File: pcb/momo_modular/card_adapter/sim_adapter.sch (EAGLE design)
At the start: 6 parts, among them U1 ESDA6V1SC6

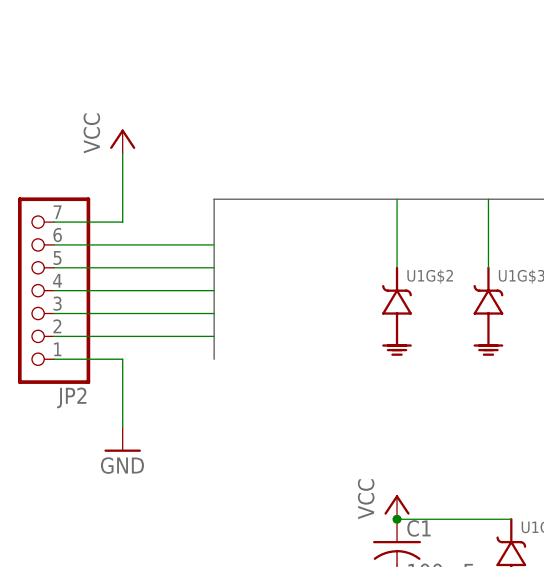
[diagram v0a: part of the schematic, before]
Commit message: Finalize sd/sim card adapter board
- make size a round number
- make pinout standard for minimal wiring
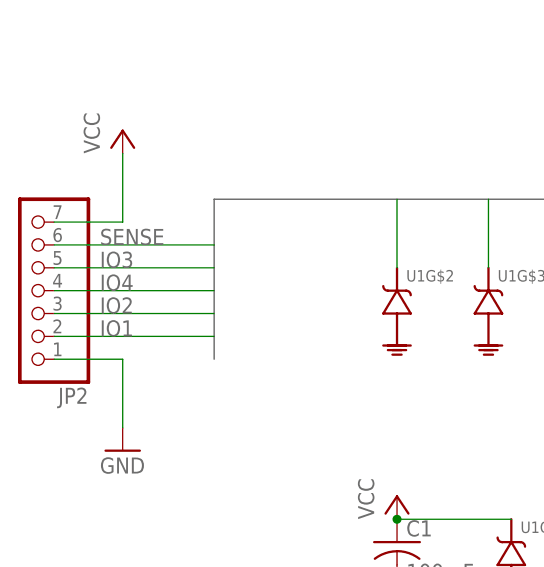
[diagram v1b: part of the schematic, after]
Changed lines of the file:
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@@
 <?xml version="1.0" encoding="utf-8"?>
 <!DOCTYPE eagle SYSTEM "eagle.dtd">
-<eagle version="6.5.0">
+<eagle version="6.4">
 <drawing>
 <settings>
@@
 <pinref part="JP2" gate="A" pin="2"/>
 <wire x1="33.02" y1="106.68" x2="15.24" y2="106.68" width="0.1524" layer="91"/>
+<label x="20.32" y="106.68" size="1.778" layer="95"/>
 </segment>
 </net>
@@
 <pinref part="JP2" gate="A" pin="3"/>
 <wire x1="33.02" y1="109.22" x2="15.24" y2="109.22" width="0.1524" layer="91"/>
+<label x="20.32" y="109.22" size="1.778" layer="95"/>
 </segment>
 </net>
@@
 <pinref part="JP2" gate="A" pin="5"/>
 <wire x1="33.02" y1="114.3" x2="15.24" y2="114.3" width="0.1524" layer="91"/>
+<label x="20.32" y="114.3" size="1.778" layer="95"/>
 </segment>
 </net>
@@
 <pinref part="JP2" gate="A" pin="4"/>
 <wire x1="33.02" y1="111.76" x2="15.24" y2="111.76" width="0.1524" layer="91"/>
+<label x="20.32" y="111.76" size="1.778" layer="95"/>
 </segment>
 </net>
@@
 <pinref part="JP2" gate="A" pin="6"/>
 <wire x1="33.02" y1="116.84" x2="15.24" y2="116.84" width="0.1524" layer="91"/>
-</segment>
-</net>
+<label x="20.32" y="116.84" size="1.778" layer="95"/>
+</segment>
+</net>

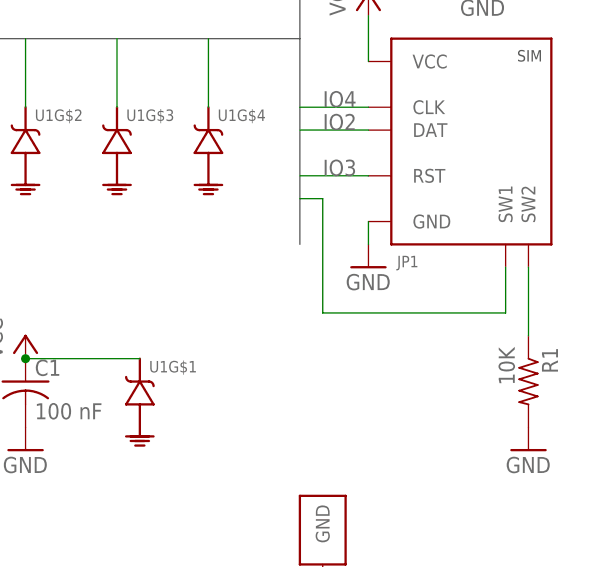
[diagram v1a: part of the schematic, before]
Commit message: Add final wire for sensing sim insertion
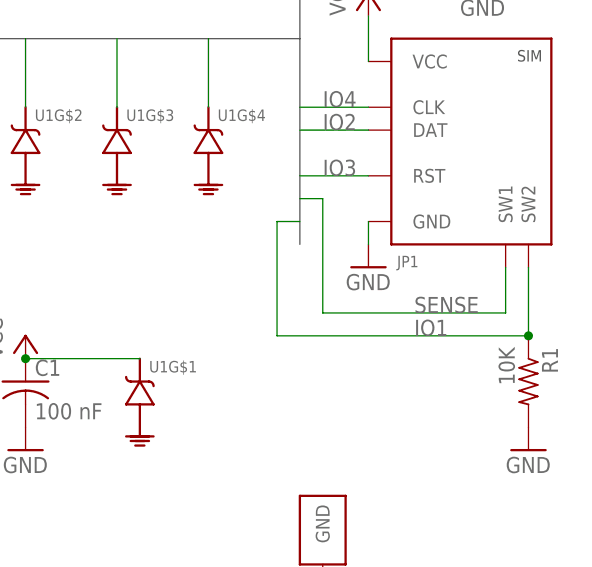
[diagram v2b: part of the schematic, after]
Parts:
- C1: DIGIKEY-PN (none) -> 445-1265-1-ND
- JP3: POPULATE-SIM (none) -> no
- R1: DIGIKEY-PN (none) -> P10.0KHCT-ND
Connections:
- removed net N$1: JP1.SW2, R1.1
- net IO1: now also JP1.SW2, R1.1
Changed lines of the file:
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@@
 <?xml version="1.0" encoding="utf-8"?>
 <!DOCTYPE eagle SYSTEM "eagle.dtd">
-<eagle version="6.4">
+<eagle version="6.5.0">
 <drawing>
 <settings>
@@
 <attribute name="DIGIKEY-PN-SD" value=""/>
 </part>
-<part name="R1" library="rcl" deviceset="R-US_" device="R0603" value="10K"/>
-<part name="C1" library="rcl" deviceset="C-US" device="C0402" value="100 nF"/>
+<part name="R1" library="rcl" deviceset="R-US_" device="R0603" value="10K">
+<attribute name="DIGIKEY-PN" value="P10.0KHCT-ND"/>
+</part>
+<part name="C1" library="rcl" deviceset="C-US" device="C0402" value="100 nF">
+<attribute name="DIGIKEY-PN" value="445-1265-1-ND"/>
+</part>
 <part name="GND1" library="supply1" deviceset="GND" device=""/>
 <part name="GND2" library="supply1" deviceset="GND" device=""/>
@@
 <part name="GND5" library="supply1" deviceset="GND" device=""/>
 <part name="JP3" library="components" deviceset="SDCARD-HOLDER" device="">
-<attribute name="DIGIKEY-PN-SIM" value=""/>
+<attribute name="POPULATE-SIM" value="no"/>
 </part>
 <part name="JP2" library="pinhead" deviceset="PINHD-1X7" device=""/>
@@
 <attribute name="DIGIKEY-PN-SD" x="93.98" y="106.68" size="1.778" layer="96" display="off"/>
 </instance>
-<instance part="R1" gate="G$1" x="109.22" y="83.82" rot="R270"/>
-<instance part="C1" gate="G$1" x="53.34" y="83.82"/>
+<instance part="R1" gate="G$1" x="109.22" y="83.82" rot="R270">
+<attribute name="DIGIKEY-PN" x="109.22" y="83.82" size="1.778" layer="96" rot="R270" display="off"/>
+</instance>
+<instance part="C1" gate="G$1" x="53.34" y="83.82">
+<attribute name="DIGIKEY-PN" x="53.34" y="83.82" size="1.778" layer="96" display="off"/>
+</instance>
 <instance part="GND1" gate="1" x="91.44" y="96.52"/>
 <instance part="GND2" gate="1" x="109.22" y="76.2"/>
@@
 <instance part="GND5" gate="1" x="86.36" y="55.88"/>
 <instance part="JP3" gate="G$1" x="96.52" y="149.86">
-<attribute name="DIGIKEY-PN-SIM" x="96.52" y="149.86" size="1.778" layer="96" display="off"/>
+<attribute name="POPULATE-SIM" x="96.52" y="149.86" size="1.778" layer="96" display="off"/>
 </instance>
 <instance part="JP2" gate="A" x="12.7" y="111.76" rot="R180"/>
@@
 </segment>
 </net>
-<net name="N$1" class="0">
-<segment>
+<net name="IO1" class="0">
+<segment>
+<pinref part="JP3" gate="G$1" pin="CS"/>
+<wire x1="91.44" y1="157.48" x2="83.82" y2="157.48" width="0.1524" layer="91"/>
+<label x="86.36" y="157.48" size="1.778" layer="95"/>
+</segment>
+<segment>
+<pinref part="JP2" gate="A" pin="2"/>
+<wire x1="33.02" y1="106.68" x2="15.24" y2="106.68" width="0.1524" layer="91"/>
+<label x="20.32" y="106.68" size="1.778" layer="95"/>
+</segment>
+<segment>
+<wire x1="83.82" y1="101.6" x2="81.28" y2="101.6" width="0.1524" layer="91"/>
+<wire x1="81.28" y1="101.6" x2="81.28" y2="88.9" width="0.1524" layer="91"/>
 <pinref part="JP1" gate="G$1" pin="SW2"/>
 <pinref part="R1" gate="G$1" pin="1"/>
 <wire x1="109.22" y1="96.52" x2="109.22" y2="88.9" width="0.1524" layer="91"/>
-</segment>
-</net>
-<net name="IO1" class="0">
-<segment>
-<pinref part="JP3" gate="G$1" pin="CS"/>
-<wire x1="91.44" y1="157.48" x2="83.82" y2="157.48" width="0.1524" layer="91"/>
-<label x="86.36" y="157.48" size="1.778" layer="95"/>
-</segment>
-<segment>
-<pinref part="JP2" gate="A" pin="2"/>
-<wire x1="33.02" y1="106.68" x2="15.24" y2="106.68" width="0.1524" layer="91"/>
-<label x="20.32" y="106.68" size="1.778" layer="95"/>
+<wire x1="81.28" y1="88.9" x2="109.22" y2="88.9" width="0.1524" layer="91"/>
+<junction x="109.22" y="88.9"/>
+<label x="96.52" y="88.9" size="1.778" layer="95"/>
 </segment>
 </net>
@@
 <wire x1="106.68" y1="96.52" x2="106.68" y2="91.44" width="0.1524" layer="91"/>
 <wire x1="86.36" y1="91.44" x2="106.68" y2="91.44" width="0.1524" layer="91"/>
-</segment>
-<segment>
+<label x="96.52" y="91.44" size="1.778" layer="95"/>
+</segment>
+<segment>
